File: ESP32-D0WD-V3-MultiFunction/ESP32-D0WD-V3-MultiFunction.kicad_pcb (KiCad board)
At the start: 2 copper layers, 104.1 x 127 mm, 144 parts, among them J201 Programming Header, J801 RJ45, J802 RJ45, P701 A7 A6 A5 A4 A3 A2 A1 A0 C, P702 B7 B6 B5 B4 B3 B2 B1 B0 C, SW201 RESET, T701 + 12V -, T801 - 15 in +, T802 - 15 out +, U201 ESP32-D0WD-V3, U202 W25Q32JVSSIQ, U301 LM2574N-3.3, U401 TC4426, U402 TC4426, U403 74HCT14, U501 74HCT00, U502 74HCT00, U503 TC4428, U504 TC4428, U505 TC4428, U506 TC4428, U601 LM339, U602 LM339, U701 PCA9685, U702 TBD62X83A, U703 TBD62X83A, U801 TCAN332DR, Y201 40 Mhz +/- 10 ppm

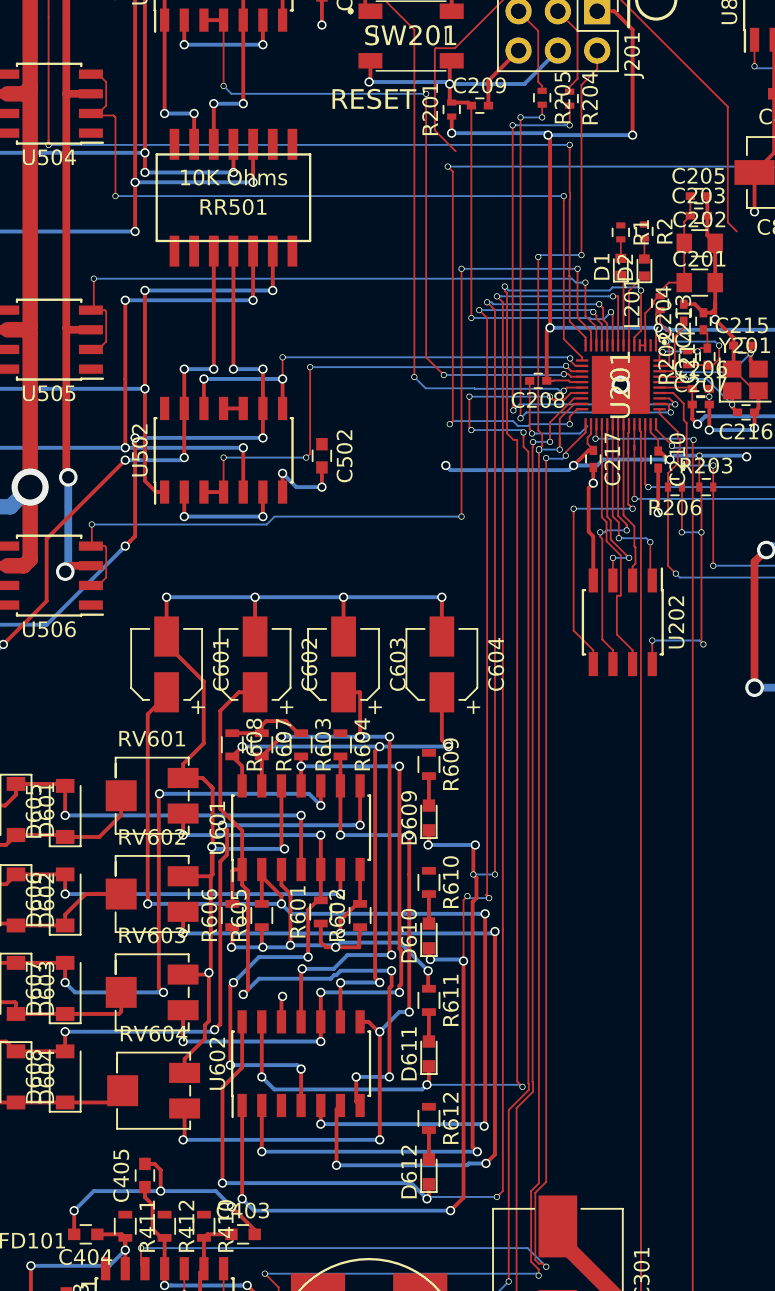
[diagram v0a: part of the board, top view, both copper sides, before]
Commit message: Fix incorrect I/O pin assignments.
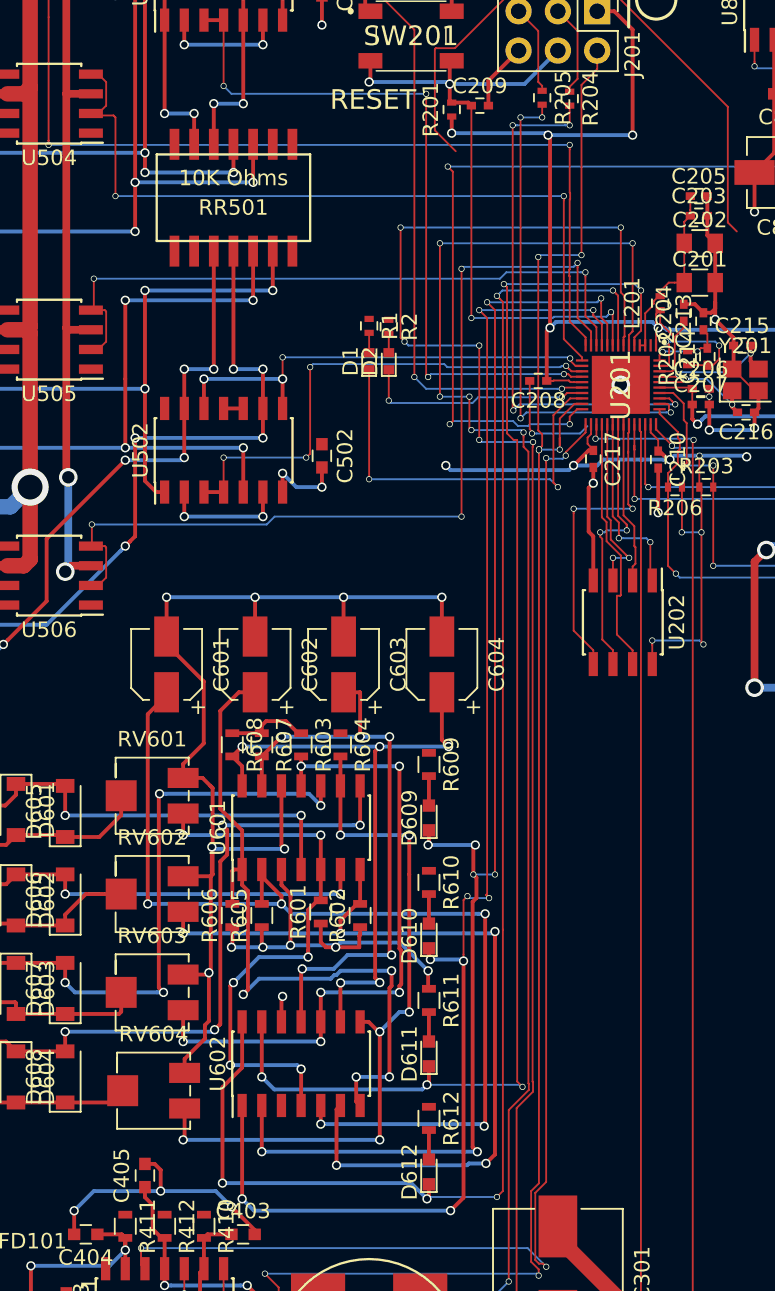
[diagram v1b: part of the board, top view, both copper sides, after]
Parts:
- moved R2 17.6 mm to (113.5, 70.9)
- moved D2 17.6 mm to (113.5, 73.2)
- moved D1 17.4 mm to (112.3, 73.2)
- moved R1 17.3 mm to (112.3, 70.9)
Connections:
- D1 pad 1: /ESP32 MCU/GPIO38(Act2) -> /ESP32 MCU/GPIO2(Act2)
- D2 pad 1: /ESP32 MCU/GPIO37(Act1) -> /ESP32 MCU/GPIO15(Act1)
- U201 pad 21: /Buttons and LEDs/Button3 -> /ESP32 MCU/GPIO15(Act1)
- U201 pad 22: /Buttons and LEDs/Button2 -> /ESP32 MCU/GPIO2(Act2)
- U201 pad 6: /ESP32 MCU/GPIO37(Act1) -> /Buttons and LEDs/Button3
- U201 pad 7: /ESP32 MCU/GPIO38(Act2) -> /Buttons and LEDs/Button2
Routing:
- net /Buttons and LEDs/Button2: track 82.0 -> 121.0 mm, vias 4 -> 8
- net /ESP32 MCU/GPIO2(Act2): track 0.00 -> 26.5 mm, vias 0 -> 2
- net /Buttons and LEDs/Button3: track 91.6 -> 115.0 mm, vias 6 -> 8
- net /ESP32 MCU/GPIO15(Act1): track 0.00 -> 14.8 mm, vias 0 -> 2
- net /ESP32 MCU/GPIO37(Act1): track 4.92 -> 0.00 mm
- net /ESP32 MCU/GPIO38(Act2): track 4.59 -> 0.00 mm
- net /ESP32 MCU/GPIO12(Points1): track 46.5 -> 47.2 mm
- net /ESP32 MCU/GPIO32(Motor3): track 42.5 -> 43.2 mm
- net /ESP32 MCU/GPIO33(Motor4): track 58.5 -> 59.0 mm
- net /ESP32 MCU/GPIO34(OD1): track 89.8 -> 90.3 mm

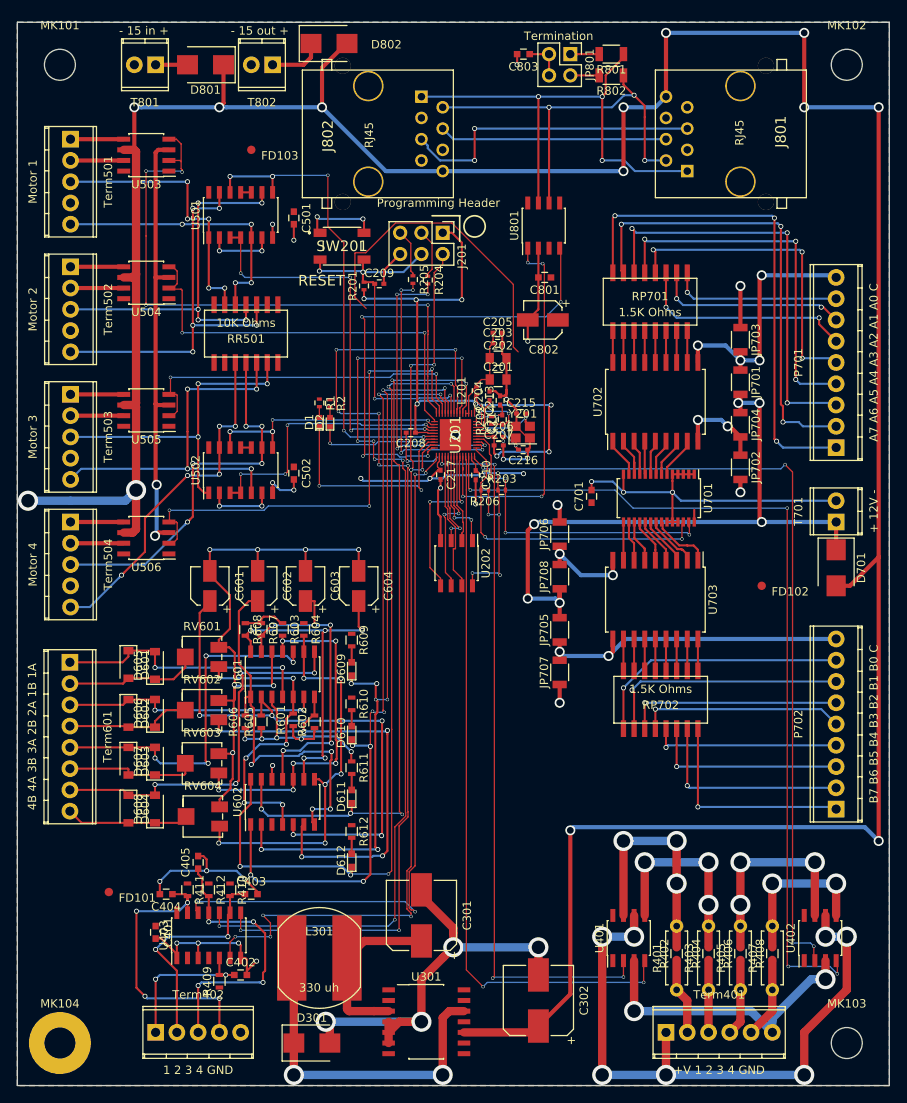
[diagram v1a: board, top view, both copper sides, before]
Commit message: Complete BOM for ESP32-D0WD-V3-MultiFunction.
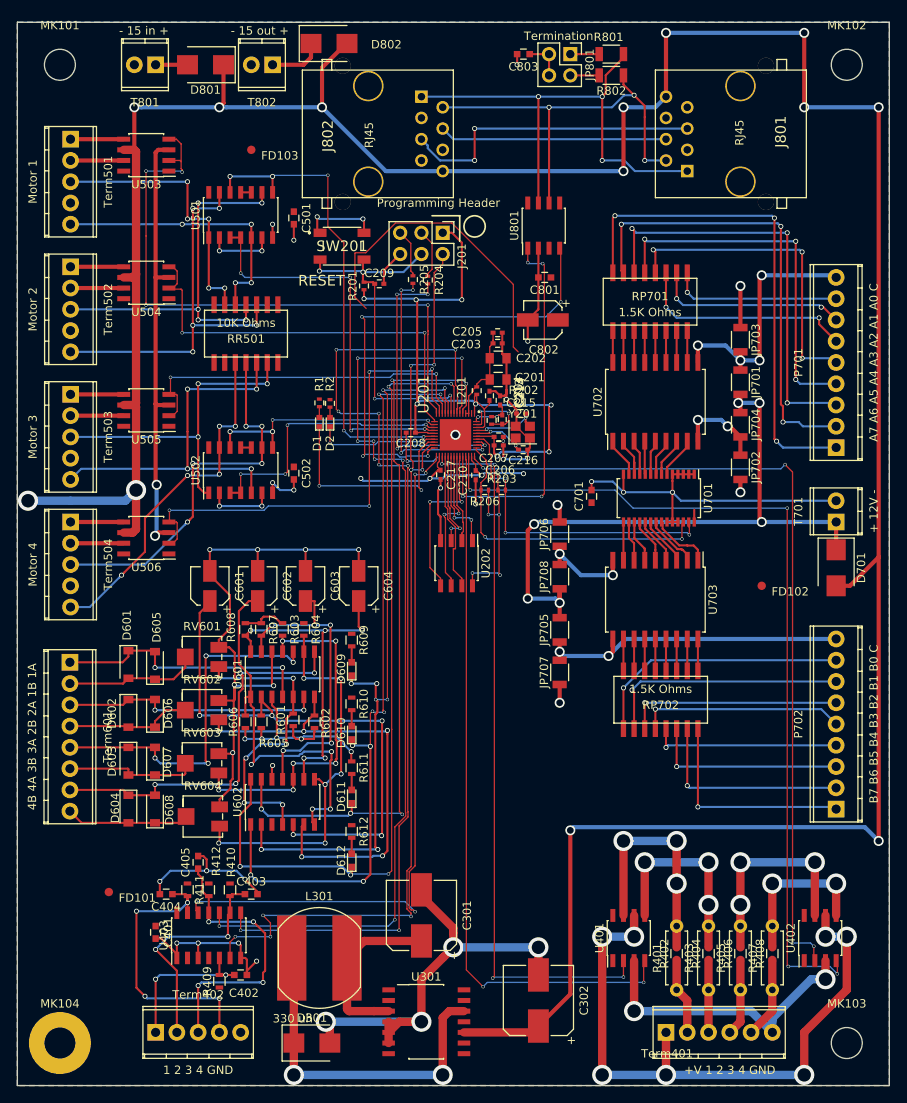
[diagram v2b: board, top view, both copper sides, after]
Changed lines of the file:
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@@
     (47 F.CrtYd user)
     (48 B.Fab user)
-    (49 F.Fab user)
+    (49 F.Fab user hide)
   )
   (setup
-    (last_trace_width 0.12)
+    (last_trace_width 0.25)
     (user_trace_width 0.12)
     (user_trace_width 0.5)
@@
     (tags "resistor 0402")
     (attr smd)
-    (fp_text reference R2 (at 0 -1.35 270) (layer F.SilkS)
+    (fp_text reference R2 (at -2.344 0 270) (layer F.SilkS)
       (effects (font (size 1 1) (thickness 0.15)))
     )
@@
     (tags "capacitor 0402")
     (attr smd)
-    (fp_text reference C210 (at 0 -1.27 270) (layer F.SilkS)
+    (fp_text reference C210 (at 0.635 1.524 270) (layer F.SilkS)
       (effects (font (size 1 1) (thickness 0.15)))
     )
@@
     (tags "capacitor 0805")
     (attr smd)
-    (fp_text reference C201 (at 0 -1.5) (layer F.SilkS)
+    (fp_text reference C201 (at 3.794 -0.254) (layer F.SilkS)
       (effects (font (size 1 1) (thickness 0.15)))
     )
@@
     (tags "capacitor 0805")
     (attr smd)
-    (fp_text reference C202 (at 0 -1.5) (layer F.SilkS)
+    (fp_text reference C202 (at 3.921 0) (layer F.SilkS)
       (effects (font (size 1 1) (thickness 0.15)))
     )
@@
     (tags "capacitor 0402")
     (attr smd)
-    (fp_text reference C203 (at 0 -1.27) (layer F.SilkS)
+    (fp_text reference C203 (at -3.768 0.127) (layer F.SilkS)
       (effects (font (size 1 1) (thickness 0.15)))
     )
@@
     (tags "capacitor 0402")
     (attr smd)
-    (fp_text reference C204 (at 0 -1.27 90) (layer F.SilkS)
+    (fp_text reference C204 (at 0.55 3.429 90) (layer F.SilkS)
       (effects (font (size 1 1) (thickness 0.15)))
     )
@@
     (tags "capacitor 0402")
     (attr smd)
-    (fp_text reference C205 (at 0 -1.27) (layer F.SilkS)
+    (fp_text reference C205 (at -3.641 -0.127) (layer F.SilkS)
       (effects (font (size 1 1) (thickness 0.15)))
     )
@@
     (tags "capacitor 0402")
     (attr smd)
-    (fp_text reference C206 (at 0 -1.27) (layer F.SilkS)
+    (fp_text reference C206 (at 0.169 3.937) (layer F.SilkS)
       (effects (font (size 1 1) (thickness 0.15)))
     )
@@
     (tags "capacitor 0402")
     (attr smd)
-    (fp_text reference C207 (at 0 -1.27) (layer F.SilkS)
+    (fp_text reference C207 (at -0.593 1.524) (layer F.SilkS)
       (effects (font (size 1 1) (thickness 0.15)))
     )
@@
     (tags "capacitor 0402")
     (attr smd)
-    (fp_text reference C213 (at 0 -1.27 90) (layer F.SilkS)
+    (fp_text reference C213 (at 0.847 2.286 90) (layer F.SilkS)
       (effects (font (size 1 1) (thickness 0.15)))
     )
@@
     (tags "capacitor 0402")
     (attr smd)
-    (fp_text reference C214 (at 0 -1.27 90) (layer F.SilkS)
+    (fp_text reference C214 (at 3.26 2.159 90) (layer F.SilkS)
       (effects (font (size 1 1) (thickness 0.15)))
     )
@@
     (tags "capacitor 0603")
     (attr smd)
-    (fp_text reference C402 (at 0 -1.5) (layer F.SilkS)
+    (fp_text reference C402 (at 0.393 2.159) (layer F.SilkS)
       (effects (font (size 1 1) (thickness 0.15)))
     )
@@
     (tags SOD-123)
     (attr smd)
-    (fp_text reference D601 (at 0 -2 270) (layer F.SilkS)
+    (fp_text reference D601 (at -4.694 0.18 270) (layer F.SilkS)
       (effects (font (size 1 1) (thickness 0.15)))
     )
@@
     (tags SOD-123)
     (attr smd)
-    (fp_text reference D602 (at 0 -2 270) (layer F.SilkS)
+    (fp_text reference D602 (at 0.007 1.958 270) (layer F.SilkS)
       (effects (font (size 1 1) (thickness 0.15)))
     )
@@
     (tags SOD-123)
     (attr smd)
-    (fp_text reference D603 (at 0 -2 270) (layer F.SilkS)
+    (fp_text reference D603 (at 0.007 1.958 270) (layer F.SilkS)
       (effects (font (size 1 1) (thickness 0.15)))
     )
@@
     (tags SOD-123)
     (attr smd)
-    (fp_text reference D604 (at 0 -2 270) (layer F.SilkS)
+    (fp_text reference D604 (at -0.12 1.577 270) (layer F.SilkS)
       (effects (font (size 1 1) (thickness 0.15)))
     )
@@
     (tags SOD-123)
     (attr smd)
-    (fp_text reference D605 (at 0 -2 90) (layer F.SilkS)
+    (fp_text reference D605 (at 4.565 0.201 90) (layer F.SilkS)
       (effects (font (size 1 1) (thickness 0.15)))
     )
@@
     (tags SOD-123)
     (attr smd)
-    (fp_text reference D606 (at 0 -2 90) (layer F.SilkS)
+    (fp_text reference D606 (at -0.007 1.598 90) (layer F.SilkS)
       (effects (font (size 1 1) (thickness 0.15)))
     )
@@
     (tags SOD-123)
     (attr smd)
-    (fp_text reference D607 (at 0 -2 90) (layer F.SilkS)
+    (fp_text reference D607 (at -0.134 1.471 90) (layer F.SilkS)
       (effects (font (size 1 1) (thickness 0.15)))
     )
@@
     (tags SOD-123)
     (attr smd)
-    (fp_text reference D608 (at 0 -2 90) (layer F.SilkS)
+    (fp_text reference D608 (at -0.134 1.725 90) (layer F.SilkS)
       (effects (font (size 1 1) (thickness 0.15)))
     )
@@
   (module SRN1060:SRN1060 (layer F.Cu)
     (at 112.27 137.16)
-    (fp_text reference L301 (at -0.01524 -3.1623) (layer F.SilkS)
+    (fp_text reference L301 (at -0.01524 -7.366) (layer F.SilkS)
       (effects (font (size 1 1) (thickness 0.15)))
     )
-    (fp_text value "330 uh" (at -0.0381 3.556) (layer F.SilkS)
+    (fp_text value "330 uh" (at -3.177 7.239) (layer F.SilkS)
       (effects (font (size 1 1) (thickness 0.15)))
     )
@@
     (tags "resistor 0402")
     (attr smd)
-    (fp_text reference R202 (at 0 -1.35 90) (layer F.SilkS)
+    (fp_text reference R202 (at 3.614 3.81 180) (layer F.SilkS)
       (effects (font (size 1 1) (thickness 0.15)))
     )
@@
     (tags "resistor 0603")
     (attr smd)
-    (fp_text reference R410 (at 0 -1.45 270) (layer F.SilkS)
+    (fp_text reference R410 (at -3.29 -0.127 270) (layer F.SilkS)
       (effects (font (size 1 1) (thickness 0.15)))
     )
@@
     (tags "resistor 0603")
     (attr smd)
-    (fp_text reference R412 (at 0 -1.45 270) (layer F.SilkS)
+    (fp_text reference R412 (at -3.417 -0.889 270) (layer F.SilkS)
       (effects (font (size 1 1) (thickness 0.15)))
     )
@@
     (tags "resistor 0603")
     (attr smd)
-    (fp_text reference R602 (at 0 -1.45 90) (layer F.SilkS)
+    (fp_text reference R602 (at -0.145 1.344 90) (layer F.SilkS)
       (effects (font (size 1 1) (thickness 0.15)))
     )
@@
     (tags "resistor 0603")
     (attr smd)
-    (fp_text reference R605 (at 0 -1.45 90) (layer F.SilkS)
+    (fp_text reference R605 (at -2.558 1.471 180) (layer F.SilkS)
       (effects (font (size 1 1) (thickness 0.15)))
     )
@@
     (tags "resistor 0603")
     (attr smd)
-    (fp_text reference R608 (at 0 -1.45 270) (layer F.SilkS)
+    (fp_text reference R608 (at -0.26 1.704 270) (layer F.SilkS)
       (effects (font (size 1 1) (thickness 0.15)))
     )
@@
     (tags "resistor 1206")
     (attr smd)
-    (fp_text reference R801 (at 0 -1.85 180) (layer F.SilkS)
+    (fp_text reference R801 (at 0.328 2.032 180) (layer F.SilkS)
       (effects (font (size 1 1) (thickness 0.15)))
     )
@@
     (at 153.67 146.05)
     (descr "6-way 2.54mm pitch terminal block, Phoenix MPT series")
-    (fp_text reference Term401 (at 6.35 -4.50088) (layer F.SilkS)
+    (fp_text reference Term401 (at 0.127 2.54) (layer F.SilkS)
       (effects (font (size 1 1) (thickness 0.15)))
     )
-    (fp_text value "+V 1 2 3 4 GND" (at 6.35 4.50088) (layer F.SilkS)
+    (fp_text value "+V 1 2 3 4 GND" (at 7.62 4.50088) (layer F.SilkS)
       (effects (font (size 1 1) (thickness 0.15)))
     )
@@
     (tags "Integrated Circuit")
     (attr smd)
-    (fp_text reference U201 (at 0 0 270) (layer F.SilkS)
+    (fp_text reference U201 (at -4.826 3.81 270) (layer F.SilkS)
       (effects (font (size 1.27 1.27) (thickness 0.254)))
     )
@@
     (tags "LED led 0402 SMD smd SMT smt smdled SMDLED smtled SMTLED")
     (attr smd)
-    (fp_text reference D1 (at 0 -1.2 90) (layer F.SilkS)
+    (fp_text reference D1 (at -2.54 -0.254 90) (layer F.SilkS)
       (effects (font (size 1 1) (thickness 0.15)))
     )
-    (fp_text value ACT2 (at 0 1.4 90) (layer F.Fab)
+    (fp_text value ACT2 (at -2.794 -0.254 90) (layer F.Fab)
       (effects (font (size 1 1) (thickness 0.15)))
     )
@@
     (tags "LED led 0402 SMD smd SMT smt smdled SMDLED smtled SMTLED")
     (attr smd)
-    (fp_text reference D2 (at 0 -1.2 90) (layer F.SilkS)
+    (fp_text reference D2 (at -2.54 0 90) (layer F.SilkS)
       (effects (font (size 1 1) (thickness 0.15)))
     )
-    (fp_text value ACT1 (at 0 1.4 90) (layer F.Fab)
+    (fp_text value ACT1 (at -2.794 0 90) (layer F.Fab)
       (effects (font (size 1 1) (thickness 0.15)))
     )
@@
     (tags "resistor 0402")
     (attr smd)
-    (fp_text reference R1 (at 0 -1.35 270) (layer F.SilkS)
+    (fp_text reference R1 (at -2.286 0 270) (layer F.SilkS)
       (effects (font (size 1 1) (thickness 0.15)))
     )
